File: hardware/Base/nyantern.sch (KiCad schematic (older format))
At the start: 23 parts, among them U1 TP4056board, U2 MT3608board, U3 WeMos_mini, U4 MPU6050board

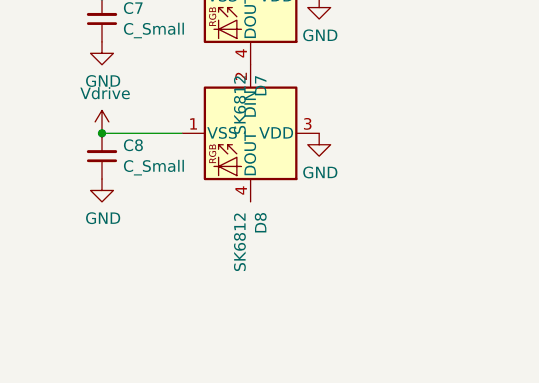
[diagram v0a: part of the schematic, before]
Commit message: Added reflective copper on inside Added version with cutout dinoskin Generated gerbers
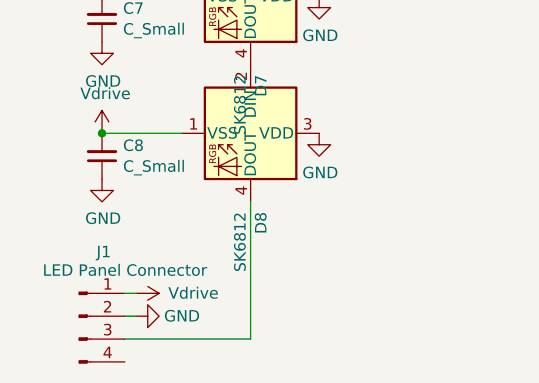
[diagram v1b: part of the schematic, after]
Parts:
- added J1: LED Panel Connector, Connector_PinSocket_2.54mm:PinSocket_1x04_P2.54mm_Vertical, symbol Connector:Conn_01x04_Male
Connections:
- net GND: now also J1.2 (Pin_2)
- net Vdrive: now also J1.1 (Pin_1)
- net at D8.4 (DOUT): now also J1.3 (Pin_3)
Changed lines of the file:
@@
 Wire Wire Line
 	3300 4000 3400 4000
+$Comp
+L Connector:Conn_01x04_Male J1
+U 1 1 5F7E570D
+P 550 6250
+F 0 "J1" H 658 6531 50  0000 C CNN
+F 1 "LED Panel Connector" H 750 6450 50  0000 C CNN
+F 2 "Connector_PinSocket_2.54mm:PinSocket_1x04_P2.54mm_Vertical" H 550 6250 50  0001 C CNN
+F 3 "~" H 550 6250 50  0001 C CNN
+	1    550  6250
+	1    0    0    -1
+$EndComp
+$Comp
+L power:Vdrive #PWR0139
+U 1 1 5F7E72B2
+P 800 6150
+F 0 "#PWR0139" H 600 6000 50  0001 C CNN
+F 1 "Vdrive" V 800 6400 50  0000 C CNN
+F 2 "" H 800 6150 50  0001 C CNN
+F 3 "" H 800 6150 50  0001 C CNN
+	1    800  6150
+	0    1    1    0
+$EndComp
+$Comp
+L power:GND #PWR0140
+U 1 1 5F7E8644
+P 800 6250
+F 0 "#PWR0140" H 800 6000 50  0001 C CNN
+F 1 "GND" V 800 6050 50  0000 C CNN
+F 2 "" H 800 6250 50  0001 C CNN
+F 3 "" H 800 6250 50  0001 C CNN
+	1    800  6250
+	0    -1   -1   0
+$EndComp
+Wire Wire Line
+	1300 5750 1300 6350
+Wire Wire Line
+	1300 6350 750  6350
+Wire Wire Line
+	750  6250 800  6250
+Wire Wire Line
+	800  6150 750  6150
 $EndSCHEMATC
